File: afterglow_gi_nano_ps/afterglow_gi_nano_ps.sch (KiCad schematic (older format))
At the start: 64 parts, among them J1 Conn_02x17_Odd_Even, J2 POWER_CONN, J3 GI_WPC_J120, J4 GI_WPC_J121, J5 GI_CONN_J119, J6 Conn_01x12_Male, Q1 FQP30N06L, Q2 FQP30N06L, Q3 FQP30N06L, Q4 FQP30N06L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

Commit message: Added 5V stabilizing capacitor
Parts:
- added C9: 100uF, Capacitors_THT:CP_Radial_D8.0mm_P3.50mm, symbol Device:CP
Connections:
- net 5V: now also C9.1
- net GND: now also C9.2
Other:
- moved on the sheet: F1, F2, F3, F4, F5, J3, J4, J5

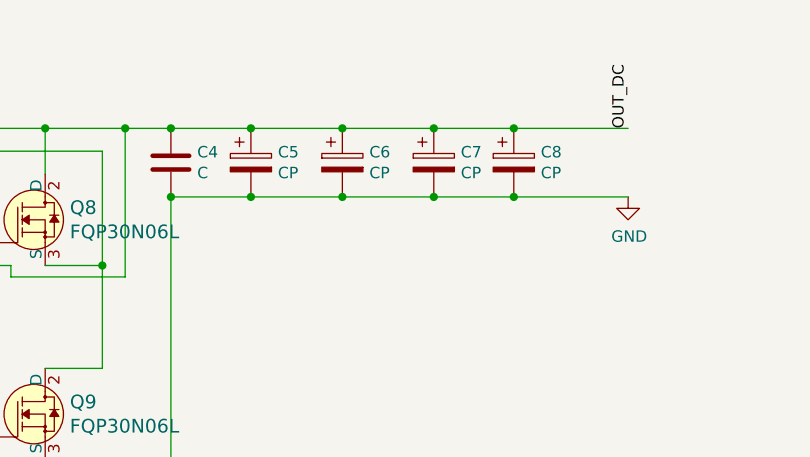
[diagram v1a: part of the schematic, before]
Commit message: Added PS BOM and schematic
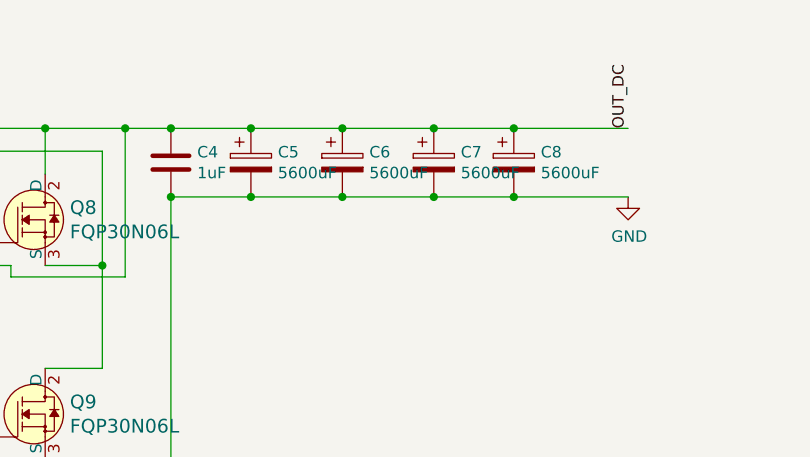
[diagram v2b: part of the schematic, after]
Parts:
- C4: value C -> 1uF
- C5, C6, C7, C8: value CP -> 5600uF
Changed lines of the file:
@@
 P 9450 1200
 F 0 "C5" H 9568 1246 50  0000 L CNN
-F 1 "CP" H 9568 1155 50  0000 L CNN
+F 1 "5600uF" H 9568 1155 50  0000 L CNN
 F 2 "Capacitors_THT:CP_Radial_D18.0mm_P7.50mm" H 9488 1050 50  0001 C CNN
 F 3 "~" H 9450 1200 50  0001 C CNN
@@
 P 9850 1200
 F 0 "C6" H 9968 1246 50  0000 L CNN
-F 1 "CP" H 9968 1155 50  0000 L CNN
+F 1 "5600uF" H 9968 1155 50  0000 L CNN
 F 2 "Capacitors_THT:CP_Radial_D18.0mm_P7.50mm" H 9888 1050 50  0001 C CNN
 F 3 "~" H 9850 1200 50  0001 C CNN
@@
 P 10250 1200
 F 0 "C7" H 10368 1246 50  0000 L CNN
-F 1 "CP" H 10368 1155 50  0000 L CNN
+F 1 "5600uF" H 10368 1155 50  0000 L CNN
 F 2 "Capacitors_THT:CP_Radial_D18.0mm_P7.50mm" H 10288 1050 50  0001 C CNN
 F 3 "~" H 10250 1200 50  0001 C CNN
@@
 P 10600 1200
 F 0 "C8" H 10718 1246 50  0000 L CNN
-F 1 "CP" H 10718 1155 50  0000 L CNN
+F 1 "5600uF" H 10718 1155 50  0000 L CNN
 F 2 "Capacitors_THT:CP_Radial_D18.0mm_P7.50mm" H 10638 1050 50  0001 C CNN
 F 3 "~" H 10600 1200 50  0001 C CNN
@@
 P 9100 1200
 F 0 "C4" H 9215 1246 50  0000 L CNN
-F 1 "C" H 9215 1155 50  0000 L CNN
+F 1 "1uF" H 9215 1155 50  0000 L CNN
 F 2 "Capacitors_THT:C_Rect_L7.0mm_W3.5mm_P5.00mm" H 9138 1050 50  0001 C CNN
 F 3 "~" H 9100 1200 50  0001 C CNN

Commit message: Some labelling
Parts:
- C1: value C_Small -> 0.1uF
- D6: value D -> 1N4004
- F1, F2, F3, F4, F5: value Fuse -> 2A
- F6: value Fuse -> 10A
- Q6, Q7, Q8, Q9: value FQP30N06L -> IRLB3813PBF
- RV1: value R_POT_TRIM -> 100k
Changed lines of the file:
@@
 P 5550 3850
 F 0 "RV1" H 5481 3896 50  0000 R CNN
-F 1 "R_POT_TRIM" H 5481 3805 50  0000 R CNN
+F 1 "100k" H 5481 3805 50  0000 R CNN
 F 2 "Potentiometers:Potentiometer_Trimmer_Piher_PT-10v10_Horizontal_Px10.0mm_Py5.0mm" H 5550 3850 50  0001 C CNN
 F 3 "~" H 5550 3850 50  0001 C CNN
@@
 $EndComp
 $Comp
-L Device:Fuse F1
-U 1 1 5C2F922F
-P 8800 3750
-F 0 "F1" V 8603 3750 50  0000 C CNN
-F 1 "Fuse" V 8694 3750 50  0000 C CNN
-F 2 "Fuse_Holders_and_Fuses:Fuseholder5x20_horiz_open_lateral_Type-II" V 8730 3750 50  0001 C CNN
-F 3 "~" H 8800 3750 50  0001 C CNN
-	1    8800 3750
-	0    1    1    0
-$EndComp
-$Comp
 L power:GND #PWR0101
 U 1 1 5C2F945E
@@
 P 2100 3550
 F 0 "C1" V 1871 3550 50  0000 C CNN
-F 1 "C_Small" V 1962 3550 50  0000 C CNN
+F 1 "0.1uF" V 1962 3550 50  0000 C CNN
 F 2 "Capacitors_SMD:C_0805_HandSoldering" H 2100 3550 50  0001 C CNN
 F 3 "~" H 2100 3550 50  0001 C CNN
@@
 NoConn ~ 10650 3850
 $Comp
-L Device:Fuse F2
-U 1 1 5C35316F
-P 8800 3850
-F 0 "F2" V 8603 3850 50  0000 C CNN
-F 1 "Fuse" V 8694 3850 50  0000 C CNN
-F 2 "Fuse_Holders_and_Fuses:Fuseholder5x20_horiz_open_lateral_Type-II" V 8730 3850 50  0001 C CNN
-F 3 "~" H 8800 3850 50  0001 C CNN
-	1    8800 3850
-	0    1    1    0
-$EndComp
-$Comp
 L Device:Fuse F3
 U 1 1 5C3531A3
 P 8800 3950
-F 0 "F3" V 8603 3950 50  0000 C CNN
-F 1 "Fuse" V 8694 3950 50  0000 C CNN
+F 0 "F3" V 8750 3750 50  0000 C CNN
+F 1 "2A" V 8800 3950 50  0000 C CNN
 F 2 "Fuse_Holders_and_Fuses:Fuseholder5x20_horiz_open_lateral_Type-II" V 8730 3950 50  0001 C CNN
 F 3 "~" H 8800 3950 50  0001 C CNN
@@
 U 1 1 5C3531DD
 P 8800 4050
-F 0 "F4" V 8603 4050 50  0000 C CNN
-F 1 "Fuse" V 8694 4050 50  0000 C CNN
+F 0 "F4" V 8750 3850 50  0000 C CNN
+F 1 "2A" V 8800 4050 50  0000 C CNN
 F 2 "Fuse_Holders_and_Fuses:Fuseholder5x20_horiz_open_lateral_Type-II" V 8730 4050 50  0001 C CNN
 F 3 "~" H 8800 4050 50  0001 C CNN
@@
 U 1 1 5C353215
 P 8800 4150
-F 0 "F5" V 8603 4150 50  0000 C CNN
-F 1 "Fuse" V 8694 4150 50  0000 C CNN
+F 0 "F5" V 8750 3950 50  0000 C CNN
+F 1 "2A" V 8800 4150 50  0000 C CNN
 F 2 "Fuse_Holders_and_Fuses:Fuseholder5x20_horiz_open_lateral_Type-II" V 8730 4150 50  0001 C CNN
 F 3 "~" H 8800 4150 50  0001 C CNN
@@
 U 1 1 5C3DDC36
 P 6750 3350
-F 0 "D6" H 6750 3134 50  0000 C CNN
-F 1 "D" H 6750 3225 50  0000 C CNN
+F 0 "D6" H 6700 3450 50  0000 C CNN
+F 1 "1N4004" H 6750 3250 50  0000 C CNN
 F 2 "Diodes_THT:D_5W_P10.16mm_Horizontal" H 6750 3350 50  0001 C CNN
 F 3 "~" H 6750 3350 50  0001 C CNN
@@
 P 6700 2300
 F 0 "Q7" H 6808 2353 60  0000 L CNN
-F 1 "FQP30N06L" H 6808 2247 60  0000 L CNN
+F 1 "IRLB3813PBF" H 6808 2247 60  0000 L CNN
 F 2 "TO_SOT_Packages_THT:TO-220_Vertical" H 6900 2500 60  0001 L CNN
 F 3 "https://www.fairchildsemi.com/datasheets/FQ/FQP30N06L.pdf" H 6900 2600 60  0001 L CNN
@@
 P 8550 2300
 F 0 "Q9" H 8658 2353 60  0000 L CNN
-F 1 "FQP30N06L" H 8658 2247 60  0000 L CNN
+F 1 "IRLB3813PBF" H 8658 2247 60  0000 L CNN
 F 2 "TO_SOT_Packages_THT:TO-220_Vertical" H 8750 2500 60  0001 L CNN
 F 3 "https://www.fairchildsemi.com/datasheets/FQ/FQP30N06L.pdf" H 8750 2600 60  0001 L CNN
@@
 P 8550 1450
 F 0 "Q8" H 8658 1503 60  0000 L CNN
-F 1 "FQP30N06L" H 8658 1397 60  0000 L CNN
+F 1 "IRLB3813PBF" H 8658 1397 60  0000 L CNN
 F 2 "TO_SOT_Packages_THT:TO-220_Vertical" H 8750 1650 60  0001 L CNN
 F 3 "https://www.fairchildsemi.com/datasheets/FQ/FQP30N06L.pdf" H 8750 1750 60  0001 L CNN
@@
 P 6350 1800
 F 0 "Q6" H 6458 1853 60  0000 L CNN
-F 1 "FQP30N06L" H 6458 1747 60  0000 L CNN
+F 1 "IRLB3813PBF" H 6458 1747 60  0000 L CNN
 F 2 "TO_SOT_Packages_THT:TO-220_Vertical" H 6550 2000 60  0001 L CNN
 F 3 "https://www.fairchildsemi.com/datasheets/FQ/FQP30N06L.pdf" H 6550 2100 60  0001 L CNN
@@
 P 6000 1000
 F 0 "F6" V 5803 1000 50  0000 C CNN
-F 1 "Fuse" V 5894 1000 50  0000 C CNN
+F 1 "10A" V 5894 1000 50  0000 C CNN
 F 2 "Fuse_Holders_and_Fuses:Fuseholder5x20_horiz_open_lateral_Type-II" V 5930 1000 50  0001 C CNN
 F 3 "~" H 6000 1000 50  0001 C CNN
@@
 	7950 3850 7750 3850
 Connection ~ 7750 3850
+$Comp
+L Device:Fuse F2
+U 1 1 5C35316F
+P 8800 3850
+F 0 "F2" V 8750 3650 50  0000 C CNN
+F 1 "2A" V 8800 3850 50  0000 C CNN
+F 2 "Fuse_Holders_and_Fuses:Fuseholder5x20_horiz_open_lateral_Type-II" V 8730 3850 50  0001 C CNN
+F 3 "~" H 8800 3850 50  0001 C CNN
+	1    8800 3850
+	0    1    1    0
+$EndComp
+$Comp
+L Device:Fuse F1
+U 1 1 5C2F922F
+P 8800 3750
+F 0 "F1" V 8750 3550 50  0000 C CNN
+F 1 "2A" V 8800 3750 50  0000 C CNN
+F 2 "Fuse_Holders_and_Fuses:Fuseholder5x20_horiz_open_lateral_Type-II" V 8730 3750 50  0001 C CNN
+F 3 "~" H 8800 3750 50  0001 C CNN
+	1    8800 3750
+	0    1    1    0
+$EndComp
 $EndSCHEMATC
